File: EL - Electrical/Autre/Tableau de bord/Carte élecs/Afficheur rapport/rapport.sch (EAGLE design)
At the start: 15 parts, among them IC1 MCP23008P, X1 22-23-2041

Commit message: Afficheur rapport maj
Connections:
- net N$8 renamed SCL
- net N$9 renamed SDA
- removed net N$1: IC1.GP6, R3.2
- removed net N$3: IC1.GP4, R5.2
- removed net N$4: IC1.GP3, R6.2
- removed net N$6: IC1.GP1, R8.2
- removed net N$7: IC1.GP0, R9.2
- new net GP0: IC1.GP0, R5.2
- new net GP1: IC1.GP1
- new net GP2: IC1.GP2
- new net GP3: IC1.GP3, R7.2
- new net GP4: IC1.GP4, R8.2
- new net GP5: IC1.GP5, R3.2
- new net GP6: IC1.GP6, R4.2
- net GND: now also LED1.DP
- net N$2: now also R9.2; no longer IC1.GP5, R4.2
- net N$5: now also R6.2; no longer IC1.GP2, R7.2
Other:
- note added: "AILMENTATION"
- note added: "Bob Aubouin"
- note added: "Contrôleur"
- note added: "Données"
- note added: "EPSA saison 2018/2019 OPTIMUS"
- moved on the sheet: C1, C2, C3, IC1, LED1, R1, R2, R3, R4, R5, R6, R7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

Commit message: carte afficheur rapport et commandes
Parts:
- removed R3, R4, R5, R6, R7, R8, R9: 470, rcl:R-EU_0204/7
- added RA, RB, RC, RD, RE, RF, RG: 470, rcl:R-EU_0204/7
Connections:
- removed net N$2: R9.2
- removed net N$5: R6.2
- net +5V: now also LED1.DP, X1-1.S; no longer X1-2.S
- net GND: now also X1-4.S; no longer LED1.DP, X1-1.S
- net GP0: now also RC.2; no longer R5.2
- net GP1: now also RD.2
- net GP2: now also RE.2
- net GP3: now also RG.2; no longer R7.2
- net GP4: now also RF.2; no longer R8.2
- net GP5: now also RA.2; no longer R3.2
- net GP6: now also RB.2; no longer R4.2
- net N$10: now also RG.1; no longer R9.1
- net N$11: now also RF.1; no longer R8.1
- net N$12: now also RE.1; no longer R7.1
- net N$13: now also RD.1; no longer R6.1
- net N$14: now also RC.1; no longer R5.1
- net N$15: now also RB.1; no longer R4.1
- net N$16: now also RA.1; no longer R3.1
- net SCL: now also X1-2.S; no longer X1-4.S
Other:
- note added: "Affichage"
- note added: "Afficheur Rapport V1.0"
- note added: "Alimentation"
- note added: "Bob Aubouin (BAT)"
- note added: "EPSA Saison 2018/2019"
- note added: "Véhicule Optimus"
- note removed: "AILMENTATION"
- note removed: "Bob Aubouin"
- note removed: "EPSA saison 2018/2019 OPTIMUS"
- moved on the sheet: C1, C2, C3, IC1, LED1, R1, R2, X1-1, X1-2, X1-3, X1-4

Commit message: test sublime merge
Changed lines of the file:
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@@
 <part name="P+2" library="supply1" library_urn="urn:adsk.eagle:library:371" deviceset="+5V" device=""/>
 <part name="C1" library="rcl" library_urn="urn:adsk.eagle:library:334" deviceset="C-EU" device="025-025X050" package3d_urn="urn:adsk.eagle:package:23629/2" value="500pF"/>
-<part name="P+3" library="supply1" library_urn="urn:adsk.eagle:library:371" deviceset="+5V" device=""/>
 <part name="C2" library="rcl" library_urn="urn:adsk.eagle:library:334" deviceset="C-EU" device="025-025X050" package3d_urn="urn:adsk.eagle:package:23629/2" value="135pF"/>
 <part name="GND4" library="supply1" library_urn="urn:adsk.eagle:library:371" deviceset="GND" device=""/>
@@
 <part name="RG" library="rcl" library_urn="urn:adsk.eagle:library:334" deviceset="R-EU_" device="0204/7" package3d_urn="urn:adsk.eagle:package:23498/1" value="470"/>
 <part name="FRAME1" library="frames" library_urn="urn:adsk.eagle:library:229" deviceset="A4L-LOC" device=""/>
+<part name="P+3" library="supply1" library_urn="urn:adsk.eagle:library:371" deviceset="+5V" device=""/>
 </parts>
 <sheets>
@@
 <instance part="P+2" gate="1" x="177.3" y="127.74"/>
 <instance part="C1" gate="G$1" x="85.28" y="131.26"/>
-<instance part="P+3" gate="1" x="184.86" y="79"/>
 <instance part="C2" gate="G$1" x="86.82" y="87.52"/>
 <instance part="GND4" gate="1" x="86.82" y="79.9"/>
@@
 <attribute name="SHEET" x="230.505" y="5.08" size="2.54" layer="94"/>
 </instance>
+<instance part="P+3" gate="1" x="185.682" y="78.21"/>
 </instances>
 <busses>
@@
 <pinref part="LED1" gate="G$1" pin="DP"/>
 <pinref part="P+3" gate="1" pin="+5V"/>
-<wire x1="182.32" y1="56.64" x2="184.86" y2="56.64" width="0.1524" layer="91"/>
-<wire x1="184.86" y1="56.64" x2="184.86" y2="76.46" width="0.1524" layer="91"/>
+<wire x1="182.32" y1="56.64" x2="185.682" y2="56.64" width="0.1524" layer="91"/>
+<wire x1="185.682" y1="56.64" x2="185.682" y2="75.67" width="0.1524" layer="91"/>
 <pinref part="LED1" gate="G$1" pin="COM@2"/>
-<wire x1="182.32" y1="69.34" x2="184.86" y2="69.34" width="0.1524" layer="91"/>
-<wire x1="184.86" y1="69.34" x2="184.86" y2="76.46" width="0.1524" layer="91"/>
-<junction x="184.86" y="76.46"/>
+<wire x1="182.32" y1="69.34" x2="185.642" y2="69.32" width="0.1524" layer="91"/>
+<wire x1="185.642" y1="69.32" x2="185.682" y2="75.67" width="0.1524" layer="91"/>
+<junction x="185.682" y="75.67"/>
 <pinref part="LED1" gate="G$1" pin="COM@1"/>
-<wire x1="182.32" y1="71.88" x2="184.86" y2="71.88" width="0.1524" layer="91"/>
-<wire x1="184.86" y1="71.88" x2="184.86" y2="76.46" width="0.1524" layer="91"/>
+<wire x1="182.32" y1="71.88" x2="185.682" y2="71.88" width="0.1524" layer="91"/>
+<wire x1="185.682" y1="71.88" x2="185.682" y2="75.67" width="0.1524" layer="91"/>
 </segment>
 </net>

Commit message: fin des carte tdb
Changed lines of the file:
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@@
 <?xml version="1.0" encoding="utf-8"?>
 <!DOCTYPE eagle SYSTEM "eagle.dtd">
-<eagle version="9.1.0">
+<eagle version="9.2.1">
 <drawing>
 <settings>
@@
 <setting verticaltext="up"/>
 </settings>
-<grid distance="0.01" unitdist="inch" unit="inch" style="lines" multiple="1" display="no" altdistance="0.01" altunitdist="inch" altunit="inch"/>
+<grid distance="0.1" unitdist="inch" unit="inch" style="lines" multiple="1" display="no" altdistance="0.01" altunitdist="inch" altunit="inch"/>
 <layers>
 <layer number="1" name="Top" color="4" fill="1" visible="no" active="no"/>
@@
 </plain>
 <instances>
-<instance part="IC1" gate="A" x="159.52" y="115.04"/>
-<instance part="LED1" gate="G$1" x="172.16" y="64.26"/>
+<instance part="IC1" gate="A" x="159.52" y="115.04" smashed="yes">
+<attribute name="NAME" x="149.36" y="128.756" size="1.778" layer="95"/>
+<attribute name="VALUE" x="149.36" y="99.292" size="1.778" layer="96"/>
+</instance>
+<instance part="LED1" gate="G$1" x="172.16" y="64.26" smashed="yes">
+<attribute name="NAME" x="167.08" y="73.785" size="1.778" layer="95"/>
+<attribute name="VALUE" x="167.08" y="52.83" size="1.778" layer="96"/>
+</instance>
 <instance part="X1" gate="-1" x="71.92" y="133.78" smashed="yes" rot="R180">
 <attribute name="NAME" x="69.38" y="134.542" size="1.524" layer="95" rot="R180"/>
 <attribute name="VALUE" x="75.984" y="131.113" size="1.778" layer="96" rot="R180"/>
 </instance>
-<instance part="X1" gate="-2" x="68.866" y="62.12" rot="R180"/>
-<instance part="X1" gate="-3" x="69.04" y="90.06" rot="R180"/>
-<instance part="X1" gate="-4" x="71.264" y="126.18" rot="R180"/>
-<instance part="GND1" gate="1" x="95.44" y="123.64"/>
-<instance part="GND2" gate="1" x="144.28" y="102.34"/>
-<instance part="GND3" gate="1" x="139.2" y="112.5"/>
-<instance part="P+1" gate="1" x="97.98" y="136.34"/>
-<instance part="P+2" gate="1" x="177.3" y="127.74"/>
-<instance part="C1" gate="G$1" x="85.28" y="131.26"/>
-<instance part="C2" gate="G$1" x="86.82" y="87.52"/>
-<instance part="GND4" gate="1" x="86.82" y="79.9"/>
-<instance part="C3" gate="G$1" x="86.82" y="59.58"/>
-<instance part="GND5" gate="1" x="86.82" y="51.96"/>
-<instance part="P+4" gate="1" x="86.82" y="102.76"/>
-<instance part="P+6" gate="1" x="86.82" y="74.82"/>
-<instance part="R1" gate="G$1" x="86.82" y="95.14" rot="R90"/>
-<instance part="R2" gate="G$1" x="86.82" y="67.2" rot="R270"/>
-<instance part="P+5" gate="1" x="134.12" y="115.04"/>
+<instance part="X1" gate="-2" x="68.866" y="62.12" smashed="yes" rot="R180">
+<attribute name="NAME" x="66.326" y="62.882" size="1.524" layer="95" rot="R180"/>
+</instance>
+<instance part="X1" gate="-3" x="69.04" y="90.06" smashed="yes" rot="R180">
+<attribute name="NAME" x="66.5" y="90.822" size="1.524" layer="95" rot="R180"/>
+</instance>
+<instance part="X1" gate="-4" x="71.264" y="126.18" smashed="yes" rot="R180">
+<attribute name="NAME" x="68.724" y="126.942" size="1.524" layer="95" rot="R180"/>
+</instance>
+<instance part="GND1" gate="1" x="95.44" y="123.64" smashed="yes">
+<attribute name="VALUE" x="92.9" y="121.1" size="1.778" layer="96"/>
+</instance>
+<instance part="GND2" gate="1" x="144.28" y="102.34" smashed="yes">
+<attribute name="VALUE" x="141.74" y="99.8" size="1.778" layer="96"/>
+</instance>
+<instance part="GND3" gate="1" x="139.2" y="112.5" smashed="yes">
+<attribute name="VALUE" x="136.66" y="109.96" size="1.778" layer="96"/>
+</instance>
+<instance part="P+1" gate="1" x="97.98" y="136.34" smashed="yes">
+<attribute name="VALUE" x="95.44" y="131.26" size="1.778" layer="96" rot="R90"/>
+</instance>
+<instance part="P+2" gate="1" x="177.3" y="127.74" smashed="yes">
+<attribute name="VALUE" x="174.76" y="122.66" size="1.778" layer="96" rot="R90"/>
+</instance>
+<instance part="C1" gate="G$1" x="85.28" y="131.26" smashed="yes">
+<attribute name="NAME" x="86.804" y="131.641" size="1.778" layer="95"/>
+<attribute name="VALUE" x="86.804" y="126.561" size="1.778" layer="96"/>
+</instance>
+<instance part="C2" gate="G$1" x="86.82" y="87.52" smashed="yes">
+<attribute name="NAME" x="88.344" y="87.901" size="1.778" layer="95"/>
+<attribute name="VALUE" x="88.344" y="82.821" size="1.778" layer="96"/>
+</instance>
+<instance part="GND4" gate="1" x="86.82" y="79.9" smashed="yes">
+<attribute name="VALUE" x="84.28" y="77.36" size="1.778" layer="96"/>
+</instance>
+<instance part="C3" gate="G$1" x="86.82" y="59.58" smashed="yes">
+<attribute name="NAME" x="88.344" y="59.961" size="1.778" layer="95"/>
+<attribute name="VALUE" x="88.344" y="54.881" size="1.778" layer="96"/>
+</instance>
+<instance part="GND5" gate="1" x="86.82" y="51.96" smashed="yes">
+<attribute name="VALUE" x="84.28" y="49.42" size="1.778" layer="96"/>
+</instance>
+<instance part="P+4" gate="1" x="86.82" y="102.76" smashed="yes">
+<attribute name="VALUE" x="84.28" y="97.68" size="1.778" layer="96" rot="R90"/>
+</instance>
+<instance part="P+6" gate="1" x="86.82" y="74.82" smashed="yes">
+<attribute name="VALUE" x="84.28" y="69.74" size="1.778" layer="96" rot="R90"/>
+</instance>
+<instance part="R1" gate="G$1" x="86.82" y="95.14" smashed="yes" rot="R90">
+<attribute name="NAME" x="85.3214" y="91.33" size="1.778" layer="95" rot="R90"/>
+<attribute name="VALUE" x="90.122" y="91.33" size="1.778" layer="96" rot="R90"/>
+</instance>
+<instance part="R2" gate="G$1" x="86.82" y="67.2" smashed="yes" rot="R270">
+<attribute name="NAME" x="88.3186" y="71.01" size="1.778" layer="95" rot="R270"/>
+<attribute name="VALUE" x="83.518" y="71.01" size="1.778" layer="96" rot="R270"/>
+</instance>
+<instance part="P+5" gate="1" x="134.12" y="115.04" smashed="yes">
+<attribute name="VALUE" x="131.58" y="109.96" size="1.778" layer="96" rot="R90"/>
+</instance>
 <instance part="RA" gate="G$1" x="152.28" y="71.88" smashed="yes" rot="R180">
 <attribute name="NAME" x="160.17" y="73.9614" size="1.778" layer="95" rot="R180"/>
@@
 <attribute name="SHEET" x="230.505" y="5.08" size="2.54" layer="94"/>
 </instance>
-<instance part="P+3" gate="1" x="185.682" y="78.21"/>
+<instance part="P+3" gate="1" x="185.682" y="78.21" smashed="yes">
+<attribute name="VALUE" x="183.142" y="73.13" size="1.778" layer="96" rot="R90"/>
+</instance>
 </instances>
 <busses>
@@
 </sheet>
 </sheets>
+<errors>
+</errors>
 </schematic>
 </drawing>

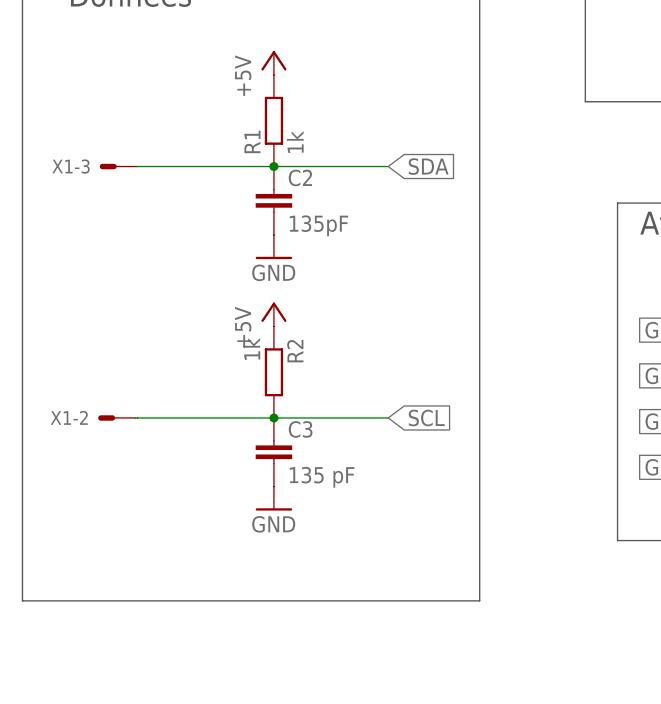
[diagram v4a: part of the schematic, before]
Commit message: modif afficheur rapport
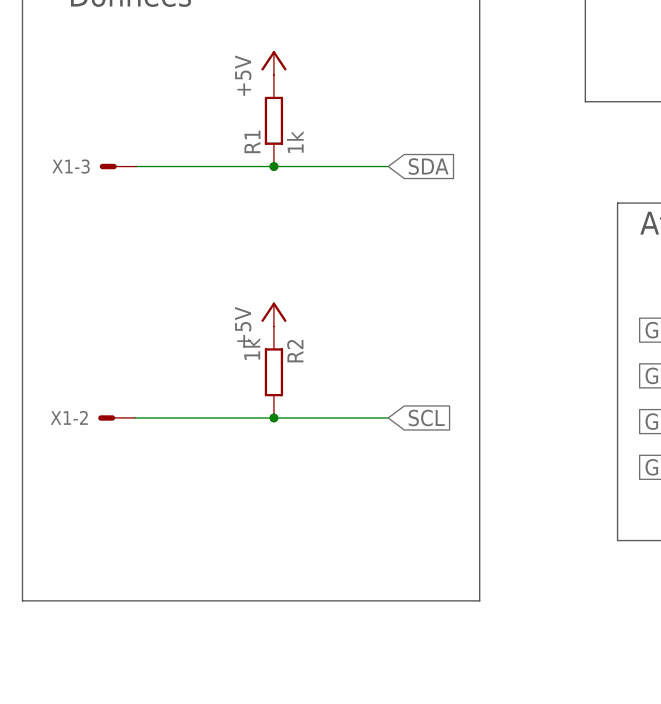
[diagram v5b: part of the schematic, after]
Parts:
- removed C2: 135pF, rcl:C-EU025-025X050
- removed C3: 135 pF, rcl:C-EU025-025X050
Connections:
- net GND: no longer C2.2, C3.2
- net SCL: no longer C3.1
- net SDA: no longer C2.1
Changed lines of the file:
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@@
 <part name="P+2" library="supply1" library_urn="urn:adsk.eagle:library:371" deviceset="+5V" device=""/>
 <part name="C1" library="rcl" library_urn="urn:adsk.eagle:library:334" deviceset="C-EU" device="025-025X050" package3d_urn="urn:adsk.eagle:package:23629/2" value="500pF"/>
-<part name="C2" library="rcl" library_urn="urn:adsk.eagle:library:334" deviceset="C-EU" device="025-025X050" package3d_urn="urn:adsk.eagle:package:23629/2" value="135pF"/>
-<part name="GND4" library="supply1" library_urn="urn:adsk.eagle:library:371" deviceset="GND" device=""/>
-<part name="C3" library="rcl" library_urn="urn:adsk.eagle:library:334" deviceset="C-EU" device="025-025X050" package3d_urn="urn:adsk.eagle:package:23629/2" value="135 pF"/>
-<part name="GND5" library="supply1" library_urn="urn:adsk.eagle:library:371" deviceset="GND" device=""/>
 <part name="P+4" library="supply1" library_urn="urn:adsk.eagle:library:371" deviceset="+5V" device=""/>
 <part name="P+6" library="supply1" library_urn="urn:adsk.eagle:library:371" deviceset="+5V" device=""/>
@@
 <attribute name="VALUE" x="86.804" y="126.561" size="1.778" layer="96"/>
 </instance>
-<instance part="C2" gate="G$1" x="86.82" y="87.52" smashed="yes">
-<attribute name="NAME" x="88.344" y="87.901" size="1.778" layer="95"/>
-<attribute name="VALUE" x="88.344" y="82.821" size="1.778" layer="96"/>
-</instance>
-<instance part="GND4" gate="1" x="86.82" y="79.9" smashed="yes">
-<attribute name="VALUE" x="84.28" y="77.36" size="1.778" layer="96"/>
-</instance>
-<instance part="C3" gate="G$1" x="86.82" y="59.58" smashed="yes">
-<attribute name="NAME" x="88.344" y="59.961" size="1.778" layer="95"/>
-<attribute name="VALUE" x="88.344" y="54.881" size="1.778" layer="96"/>
-</instance>
-<instance part="GND5" gate="1" x="86.82" y="51.96" smashed="yes">
-<attribute name="VALUE" x="84.28" y="49.42" size="1.778" layer="96"/>
-</instance>
 <instance part="P+4" gate="1" x="86.82" y="102.76" smashed="yes">
 <attribute name="VALUE" x="84.28" y="97.68" size="1.778" layer="96" rot="R90"/>
@@
 <junction x="139.2" y="117.58"/>
 </segment>
-<segment>
-<pinref part="GND4" gate="1" pin="GND"/>
-<pinref part="C2" gate="G$1" pin="2"/>
-</segment>
-<segment>
-<pinref part="C3" gate="G$1" pin="2"/>
-<pinref part="GND5" gate="1" pin="GND"/>
-</segment>
 </net>
 <net name="+5V" class="0">
@@
 <wire x1="86.82" y1="62.12" x2="99.52" y2="62.12" width="0.1524" layer="91"/>
 <pinref part="R2" gate="G$1" pin="2"/>
-<pinref part="C3" gate="G$1" pin="1"/>
 <junction x="86.82" y="62.12"/>
 <label x="99.52" y="62.12" size="1.778" layer="95" xref="yes"/>
 <pinref part="X1" gate="-2" pin="S"/>
-<wire x1="71.406" y1="62.12" x2="71.66" y2="62.12" width="0.1524" layer="91"/>
-<wire x1="71.66" y1="62.12" x2="86.82" y2="62.12" width="0.1524" layer="91"/>
+<wire x1="71.406" y1="62.12" x2="86.82" y2="62.12" width="0.1524" layer="91"/>
 </segment>
 <segment>
@@
 </segment>
 <segment>
-<pinref part="C2" gate="G$1" pin="1"/>
 <junction x="86.82" y="90.06"/>
 <pinref part="R1" gate="G$1" pin="1"/>
